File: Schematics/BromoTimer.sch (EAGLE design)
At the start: 27 parts, among them IC1 PIC16F687, IC2 7805TV, K1 351, K2 351, Q1 2N3565, Q2 2N3565, Q3 2N3565, X4 22-23-2021, X5 22-23-2021

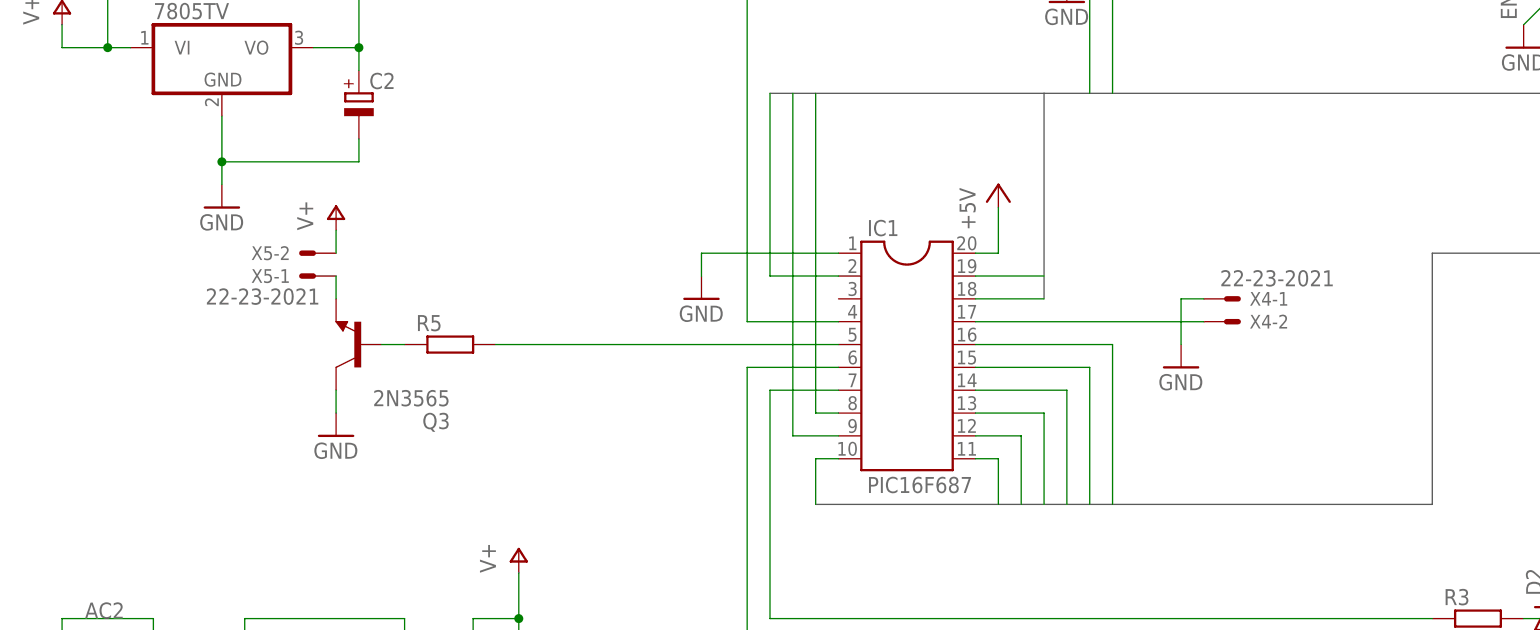
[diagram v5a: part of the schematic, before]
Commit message: Add support for external LED
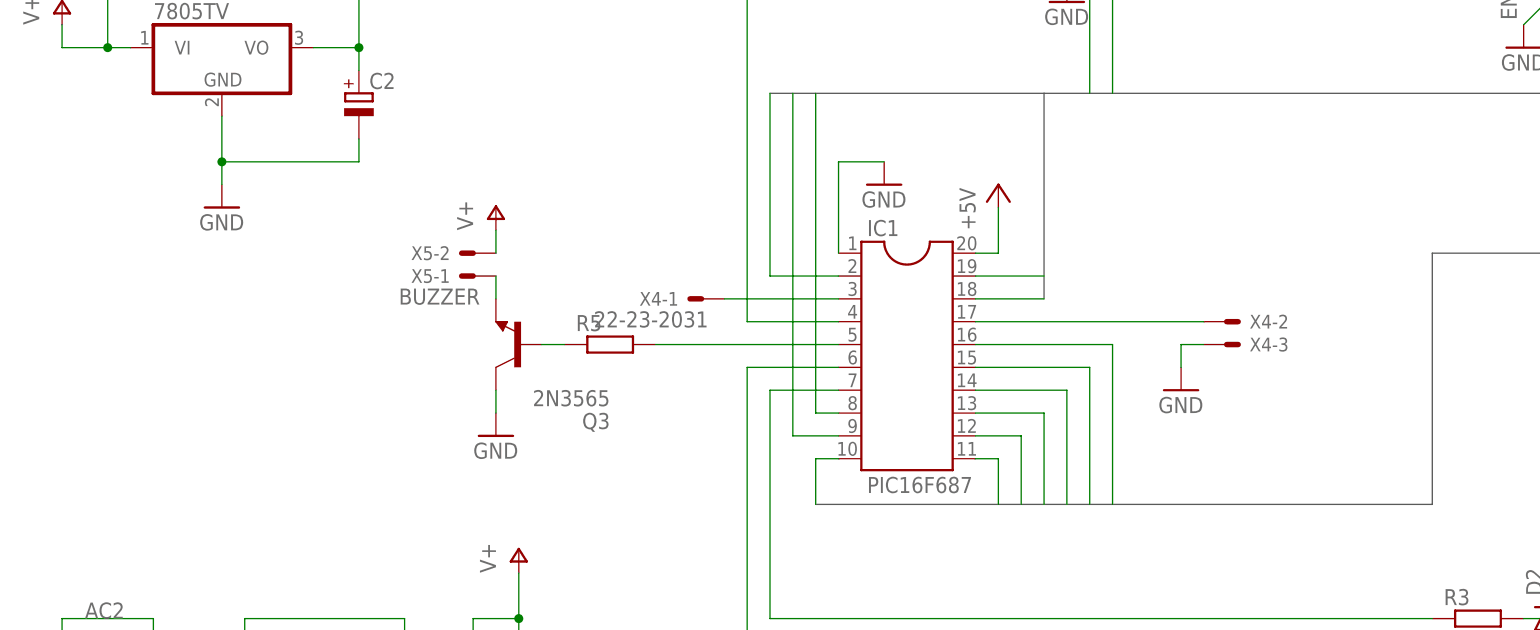
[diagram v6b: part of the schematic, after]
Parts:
- X4: value 22-23-2021 -> 22-23-2031; device con-molex:22-23-2021 -> con-molex:22-23-2031
- X5: value 22-23-2021 -> BUZZER
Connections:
- new net N$20: IC1.3, X4-1.S
- net GND: now also X4-3.S; no longer X4-1.S
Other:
- moved on the sheet: Q3, R5, X4-1, X5-1, X5-2
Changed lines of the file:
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@@
 <part name="GND7" library="supply1" deviceset="GND" device=""/>
 <part name="P+8" library="supply1" deviceset="V+" device=""/>
-<part name="X4" library="con-molex" deviceset="22-23-2021" device=""/>
 <part name="GND8" library="supply1" deviceset="GND" device=""/>
-<part name="GND9" library="supply1" deviceset="GND" device=""/>
 <part name="P+5" library="supply1" deviceset="V+" device=""/>
 <part name="P+6" library="supply1" deviceset="V+" device=""/>
@@
 <part name="R5" library="rcl" deviceset="R-EU_" device="0207/10"/>
 <part name="GND11" library="supply1" deviceset="GND" device=""/>
-<part name="X5" library="con-molex" deviceset="22-23-2021" device=""/>
+<part name="X5" library="con-molex" deviceset="22-23-2021" device="" value="BUZZER"/>
 <part name="P+10" library="supply1" deviceset="V+" device=""/>
+<part name="X4" library="con-molex" deviceset="22-23-2031" device=""/>
+<part name="GND9" library="supply1" deviceset="GND" device=""/>
 </parts>
 <sheets>
@@
 <instance part="C1" gate="G$1" x="73.66" y="81.28"/>
 <instance part="C2" gate="G$1" x="55.88" y="144.78"/>
-<instance part="GND2" gate="1" x="93.98" y="121.92"/>
+<instance part="GND2" gate="1" x="114.3" y="134.62"/>
 <instance part="P+2" gate="1" x="127" y="134.62"/>
 <instance part="GND3" gate="1" x="210.82" y="142.24"/>
@@
 <instance part="GND7" gate="1" x="73.66" y="66.04"/>
 <instance part="P+8" gate="1" x="22.86" y="154.94"/>
-<instance part="X4" gate="-1" x="152.4" y="121.92"/>
-<instance part="X4" gate="-2" x="152.4" y="119.38"/>
 <instance part="GND8" gate="1" x="185.42" y="149.86"/>
-<instance part="GND9" gate="1" x="147.32" y="114.3"/>
 <instance part="P+5" gate="1" x="205.74" y="68.58"/>
 <instance part="P+6" gate="1" x="205.74" y="111.76"/>
@@
 <instance part="GND10" gate="1" x="134.62" y="154.94"/>
 <instance part="D3" gate="G$1" x="40.64" y="160.02" rot="R180"/>
-<instance part="Q3" gate="G$1" x="55.88" y="116.84" rot="R180"/>
-<instance part="R5" gate="G$1" x="66.04" y="116.84"/>
-<instance part="GND11" gate="1" x="53.34" y="106.68"/>
-<instance part="X5" gate="-1" x="50.8" y="124.46" rot="R180"/>
-<instance part="X5" gate="-2" x="50.8" y="127" rot="R180"/>
-<instance part="P+10" gate="1" x="53.34" y="132.08"/>
+<instance part="Q3" gate="G$1" x="73.66" y="116.84" rot="R180"/>
+<instance part="R5" gate="G$1" x="83.82" y="116.84"/>
+<instance part="GND11" gate="1" x="71.12" y="106.68"/>
+<instance part="X5" gate="-1" x="68.58" y="124.46" rot="R180"/>
+<instance part="X5" gate="-2" x="68.58" y="127" rot="R180"/>
+<instance part="P+10" gate="1" x="71.12" y="132.08"/>
+<instance part="X4" gate="-1" x="93.98" y="121.92" rot="R180"/>
+<instance part="X4" gate="-2" x="152.4" y="119.38"/>
+<instance part="X4" gate="-3" x="152.4" y="116.84"/>
+<instance part="GND9" gate="1" x="147.32" y="111.76"/>
 </instances>
 <busses>
@@
 <pinref part="IC1" gate="G$1" pin="1"/>
 <pinref part="GND2" gate="1" pin="GND"/>
-<wire x1="109.22" y1="127" x2="93.98" y2="127" width="0.1524" layer="91"/>
-<wire x1="93.98" y1="127" x2="93.98" y2="124.46" width="0.1524" layer="91"/>
+<wire x1="109.22" y1="127" x2="109.22" y2="137.16" width="0.1524" layer="91"/>
+<wire x1="109.22" y1="137.16" x2="114.3" y2="137.16" width="0.1524" layer="91"/>
 </segment>
 <segment>
@@
 </segment>
 <segment>
-<pinref part="X4" gate="-1" pin="S"/>
-<pinref part="GND9" gate="1" pin="GND"/>
-<wire x1="149.86" y1="121.92" x2="147.32" y2="121.92" width="0.1524" layer="91"/>
-<wire x1="147.32" y1="121.92" x2="147.32" y2="116.84" width="0.1524" layer="91"/>
-</segment>
-<segment>
 <pinref part="SV3" gate="G$1" pin="3"/>
 <pinref part="GND10" gate="1" pin="GND"/>
@@
 <pinref part="Q3" gate="G$1" pin="C"/>
 <pinref part="GND11" gate="1" pin="GND"/>
-<wire x1="53.34" y1="111.76" x2="53.34" y2="109.22" width="0.1524" layer="91"/>
+<wire x1="71.12" y1="111.76" x2="71.12" y2="109.22" width="0.1524" layer="91"/>
+</segment>
+<segment>
+<pinref part="X4" gate="-3" pin="S"/>
+<pinref part="GND9" gate="1" pin="GND"/>
+<wire x1="149.86" y1="116.84" x2="147.32" y2="116.84" width="0.1524" layer="91"/>
+<wire x1="147.32" y1="116.84" x2="147.32" y2="114.3" width="0.1524" layer="91"/>
 </segment>
 </net>
@@
 <pinref part="P+10" gate="1" pin="V+"/>
 <pinref part="X5" gate="-2" pin="S"/>
-<wire x1="53.34" y1="129.54" x2="53.34" y2="127" width="0.1524" layer="91"/>
-</segment>
-</net>
-<net name="N$13" class="0">
-<segment>
-<pinref part="X4" gate="-2" pin="S"/>
-<pinref part="IC1" gate="G$1" pin="17"/>
-<wire x1="149.86" y1="119.38" x2="124.46" y2="119.38" width="0.1524" layer="91"/>
+<wire x1="71.12" y1="129.54" x2="71.12" y2="127" width="0.1524" layer="91"/>
 </segment>
 </net>
@@
 <pinref part="R5" gate="G$1" pin="2"/>
 <pinref part="IC1" gate="G$1" pin="5"/>
-<wire x1="71.12" y1="116.84" x2="109.22" y2="116.84" width="0.1524" layer="91"/>
+<wire x1="88.9" y1="116.84" x2="109.22" y2="116.84" width="0.1524" layer="91"/>
 </segment>
 </net>
@@
 <pinref part="R5" gate="G$1" pin="1"/>
 <pinref part="Q3" gate="G$1" pin="B"/>
-<wire x1="60.96" y1="116.84" x2="58.42" y2="116.84" width="0.1524" layer="91"/>
+<wire x1="78.74" y1="116.84" x2="76.2" y2="116.84" width="0.1524" layer="91"/>
 </segment>
 </net>
@@
 <pinref part="Q3" gate="G$1" pin="E"/>
 <pinref part="X5" gate="-1" pin="S"/>
-<wire x1="53.34" y1="124.46" x2="53.34" y2="121.92" width="0.1524" layer="91"/>
-</segment>
-</net>
+<wire x1="71.12" y1="124.46" x2="71.12" y2="121.92" width="0.1524" layer="91"/>
+</segment>
+</net>
+<net name="N$13" class="0">
+<segment>
+<pinref part="IC1" gate="G$1" pin="17"/>
+<pinref part="X4" gate="-2" pin="S"/>
+<wire x1="124.46" y1="119.38" x2="149.86" y2="119.38" width="0.1524" layer="91"/>
+</segment>
+</net>
+<net name="N$20" class="0">
+<segment>
+<pinref part="X4" gate="-1" pin="S"/>
+<pinref part="IC1" gate="G$1" pin="3"/>
+<wire x1="96.52" y1="121.92" x2="109.22" y2="121.92" width="0.1524" layer="91"/>
+</segment>
+</net>

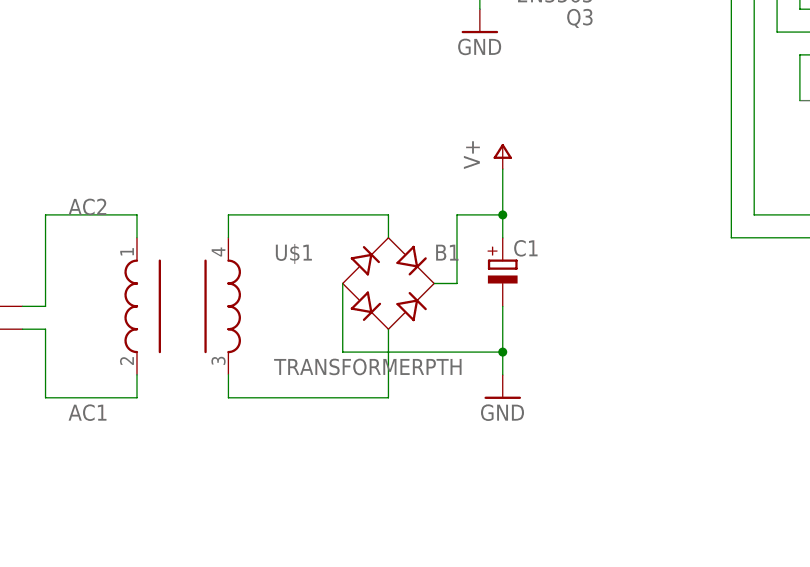
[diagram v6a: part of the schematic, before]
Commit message: Add 1n4004 diode
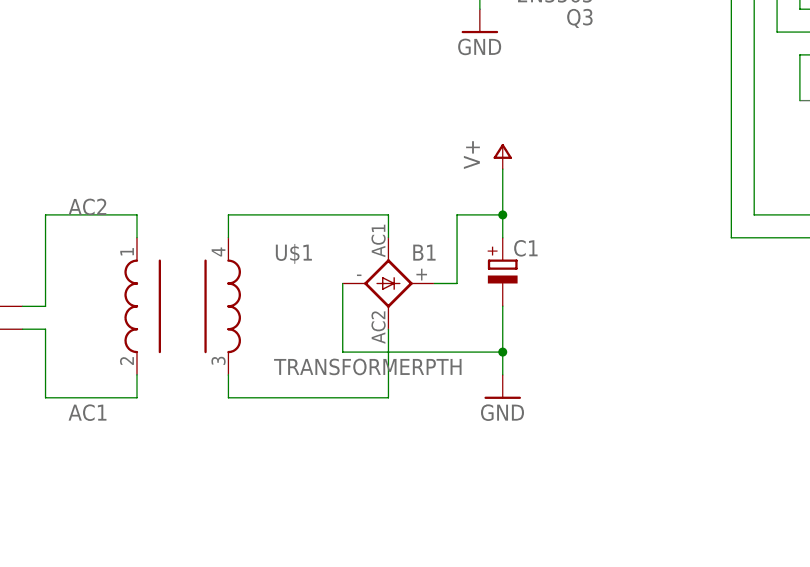
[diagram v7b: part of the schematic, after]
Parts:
- B1: device rectifier:RB1A -> rectifier:2KBB-R
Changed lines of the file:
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@@
 <part name="K2" library="relay" deviceset="351" device=""/>
 <part name="U$1" library="SparkFun" deviceset="TRANSFORMER" device="PTH"/>
-<part name="B1" library="rectifier" deviceset="RB1A" device=""/>
+<part name="B1" library="rectifier" deviceset="2KBB-R" device=""/>
 <part name="P+7" library="supply1" deviceset="V+" device=""/>
 <part name="GND7" library="supply1" deviceset="GND" device=""/>
